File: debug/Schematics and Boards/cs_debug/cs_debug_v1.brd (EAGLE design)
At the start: 83.2 x 62.2 mm, 239 parts, among them J1 J-JTAG-CORTEX_SMD, J19 Solar, J2 J-JTAG-CORTEX_SMD, J3 J-JTAG-CORTEX-NEEDLE6-LEGS, J4 J-SERIAL-PORT, J5 J-WURTH-USBC, Q10 2N7002P, Q3 FDN340P, Q4 2N7002P, Q5 FDN340P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

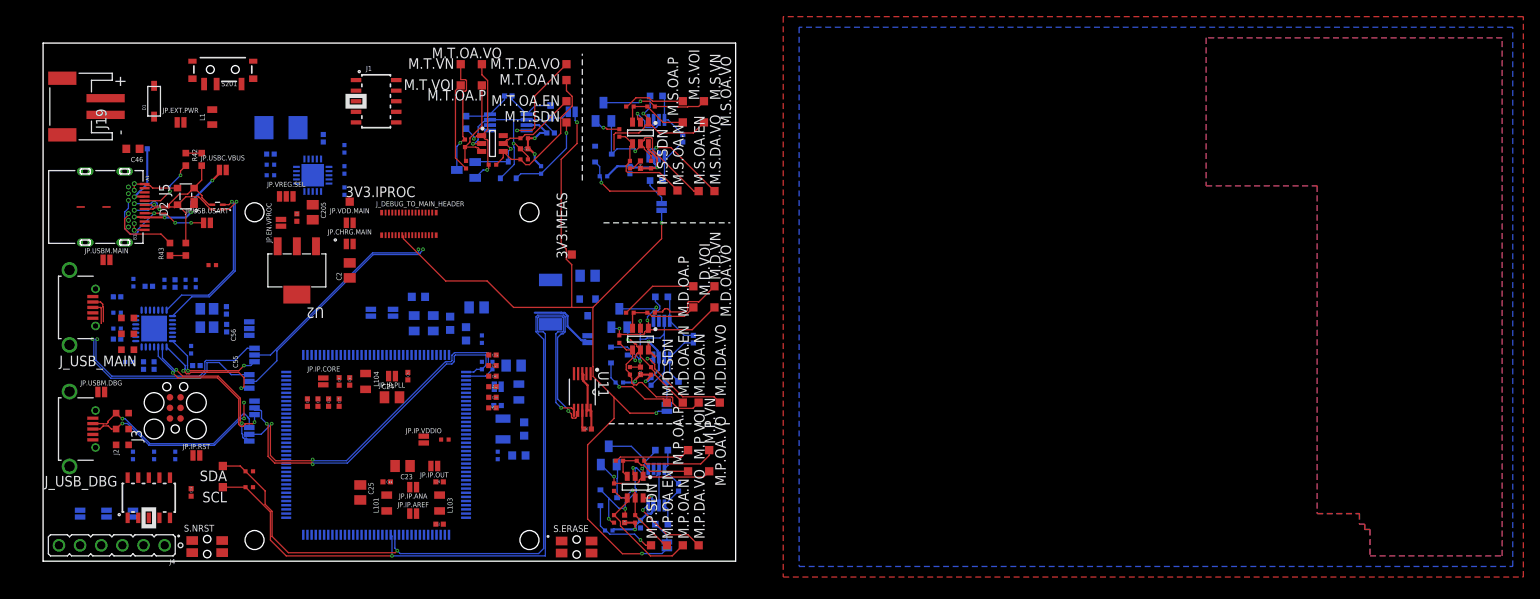
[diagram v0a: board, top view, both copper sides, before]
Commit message: DBG- analog signals hand-routed to go under 0-ohm gnd bridge
Some digital signals that went between planes were not routed under the bridge. There are the signals that  shutdown the opamp that is doing offset biasing. The signals are at about 2 levels removed from any truly analog signals, so any side-effects from ground will be  small beyond perception
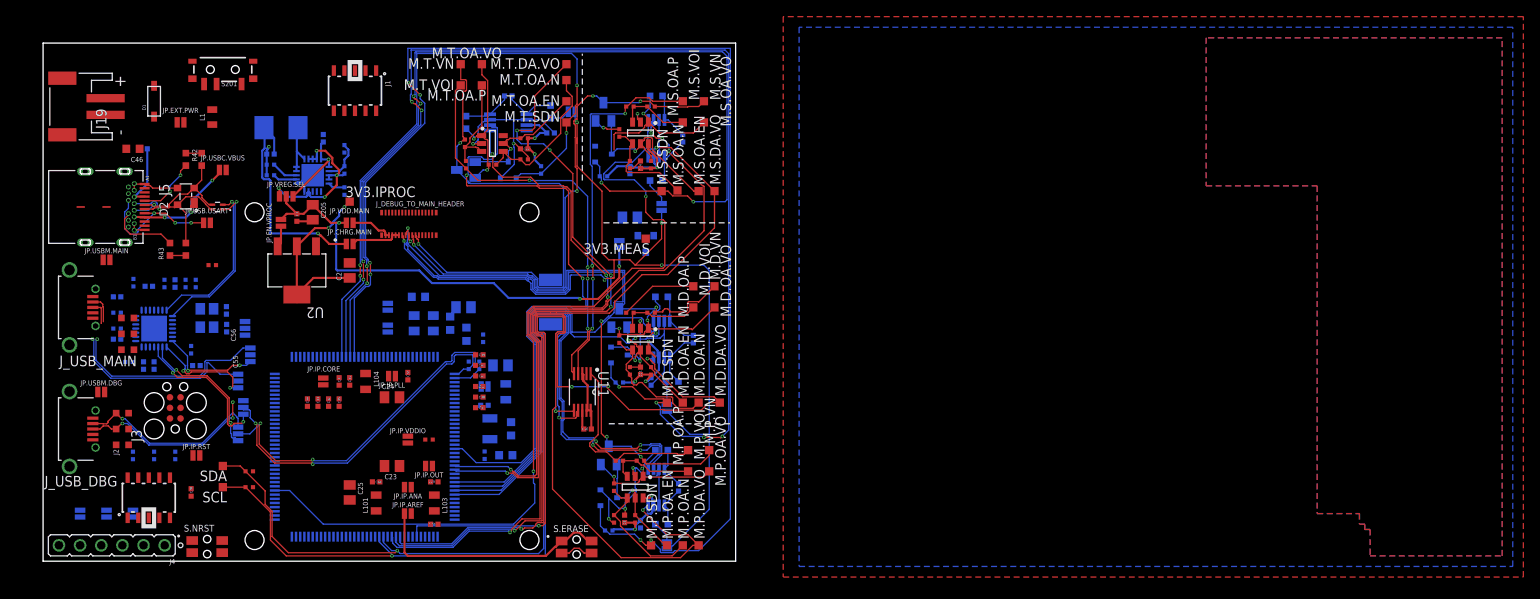
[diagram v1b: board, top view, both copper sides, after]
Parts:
- moved JP.EN.VMEAS 12.0 mm to (46.4, 38.1)
- moved U1 10.3 mm to (49.5, 38.1)
- moved 3V3.MEAS 9.09 mm to (49.5, 38.7), turned to 180 degrees
- moved C1 8.64 mm to (47.6, 41.3)
- moved J1 2.84 mm to (14.6, 56.5), turned to 180 degrees
- moved JP.UART.RX.IP 2.15 mm to (18.5, 30.6)
- moved JP.UART.TX.IP 2.01 mm to (18.5, 27.9)
- moved JP.IP.VDDIO 1.91 mm to (21.0, 14.6)
- moved R41 1.90 mm to (23.5, 14.6)
- moved C26 1.58 mm to (32.1, 23.5)
- moved C27 1.58 mm to (27.6, 30.5)
- moved C37 1.58 mm to (29.5, 18.4)
- moved C38 1.58 mm to (29.5, 19.7)
- moved C39 1.58 mm to (29.5, 24.8)
- moved C40 1.58 mm to (29.5, 23.5)
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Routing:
- net CM_PROC_DCBIAS_SHUTDOWN: track 9.48 -> 159.4 mm, vias 1 -> 6
- net CM_DTR_DCBIAS_SHUTDOWN: track 9.82 -> 147.5 mm, vias 1 -> 8
- net CM_STORAGE_DCBIAS_SHUTDOWN: track 10.4 -> 114.9 mm, vias 1 -> 6
- net CM_STORAGE_DIFFAMP_GAIN0: track 0.00 -> 102.9 mm, vias 0 -> 2
- net CM_PROC_DIFFAMP_OUT: track 9.38 -> 98.2 mm, vias 1 -> 2
- net CM_TEMP_DIFFAMP_OUT: track 12.6 -> 95.4 mm, vias 1 -> 5
- net CM_DTR_DIFFAMP_OUT: track 12.0 -> 91.0 mm, vias 1 -> 4
- net CM_STORAGE_DIFFAMP_OUT: track 10.9 -> 87.1 mm, vias 1 -> 2
- net CM_TEMP_DIFFAMP_GAIN1: track 0.00 -> 74.5 mm, vias 0 -> 2
- net CM_STORAGE_DIFFAMP_GAIN1: track 0.00 -> 72.2 mm, vias 0 -> 4
- net CM_TEMP_DIFFAMP_GAIN0: track 0.00 -> 70.7 mm, vias 0 -> 4
- net CM_TEMP_DCBIAS_SHUTDOWN: track 10.6 -> 78.5 mm, vias 1 -> 4
- net CM_PROC_DIFFAMP_GAIN0: track 0.00 -> 65.6 mm, vias 0 -> 2
- net CM_PROC_DIFFAMP_GAIN1: track 0.00 -> 64.8 mm, vias 0 -> 2
- net CM_PROC_V_SENSE_N: track 14.0 -> 72.1 mm, vias 0 -> 4
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
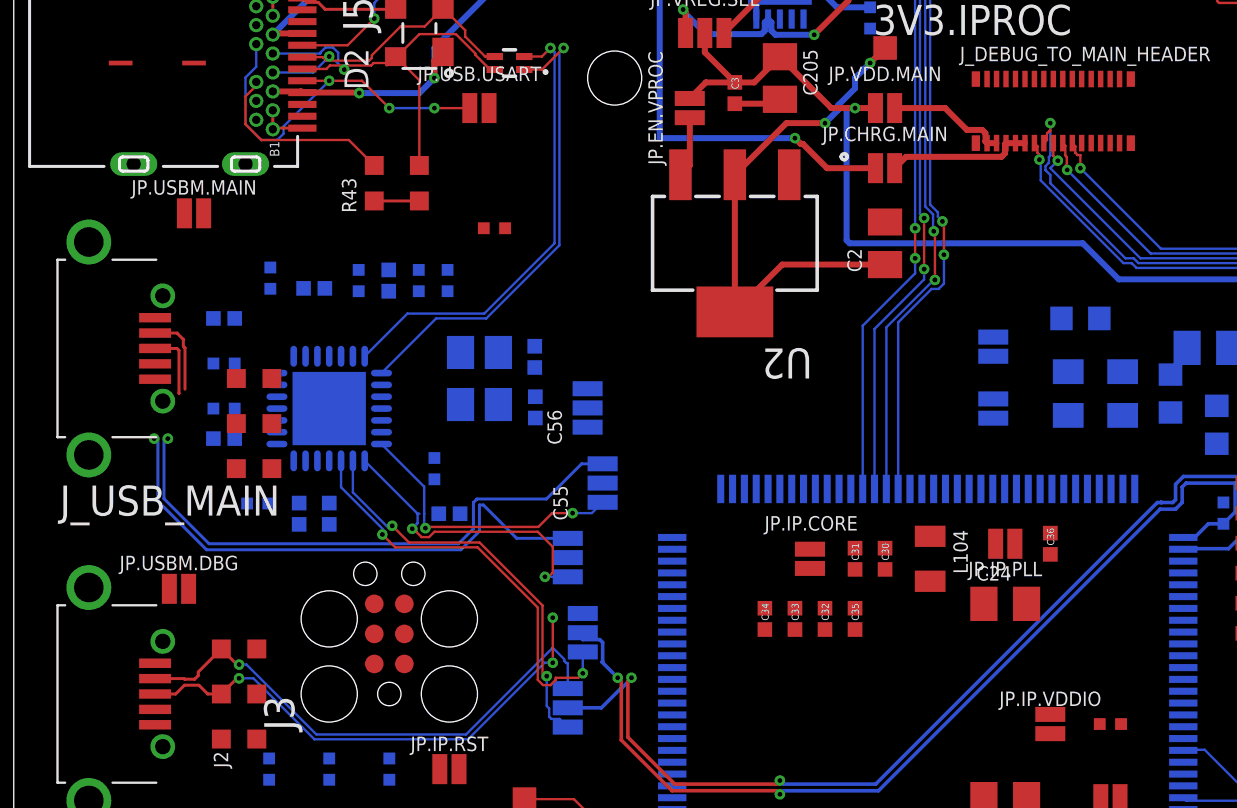
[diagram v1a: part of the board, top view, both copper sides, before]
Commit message: DBG- USB signals finished routing
Differential pairs do wonky things as they try to get identical lengths. I probably violated some rules in this regard, but it should be pretty minimal. Worst offense is the use of 3-pad solder jumpers
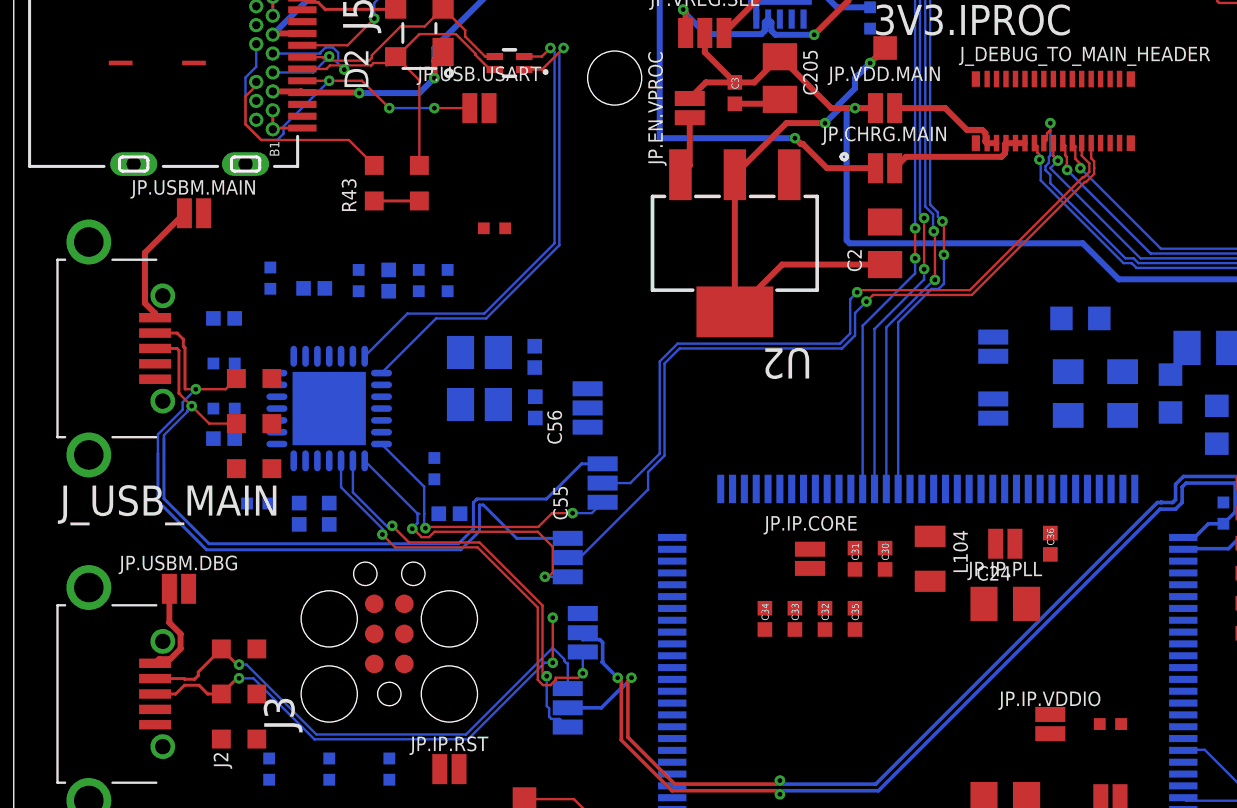
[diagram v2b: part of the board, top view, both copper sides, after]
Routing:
- net MAIN_USB_DATA_P: track 0.51 -> 33.6 mm, vias 0 -> 1
- net MAIN_USB_DATA_N: track 0.00 -> 30.5 mm, vias 0 -> 1
- net USB_BKUP_MAIN_VBUS: track 0.00 -> 5.28 mm
- net USB_BKUP_MAIN_D_N: track 26.4 -> 31.4 mm
- net USB_BKUP_MAIN_D_P: track 26.9 -> 31.6 mm
- net USB_BKUP_DBG_VBUS: track 0.00 -> 4.06 mm

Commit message: DBG - autoroute 100%
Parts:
- moved C27 0.71 mm to (27.7, 31.2)
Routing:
- net 3V3_INSTR_PROC: track 51.7 -> 239.9 mm, vias 2 -> 9
- net MAIN_USART_TX: track 0.00 -> 89.0 mm, vias 0 -> 6
- net AGND: track 85.7 -> 159.9 mm, vias 8 -> 9
- net 3V3_INSTR_MEAS: track 50.1 -> 123.0 mm, vias 8 -> 14
- net MAIN_USART_RX: track 0.00 -> 72.2 mm, vias 0 -> 5
- net VDDOUT_1: track 0.00 -> 69.1 mm, vias 0 -> 5
- net MAIN_GPIO1: track 0.00 -> 63.9 mm, vias 0 -> 5
- net MAIN_GPIO2: track 0.00 -> 61.7 mm, vias 0 -> 5
- net USB_BKUP_DBG_VBUS: track 4.06 -> 65.4 mm, vias 0 -> 1
- net MAIN_TRACE_D0/GPIO6: track 0.00 -> 61.0 mm, vias 0 -> 5
- net MAIN_TRACE_SWO/GPIO5: track 0.00 -> 60.8 mm, vias 0 -> 3
- net MAIN_TRACE_D1/GPIO7: track 0.00 -> 60.6 mm, vias 0 -> 5
- net MAIN_GPIO3: track 0.00 -> 60.4 mm, vias 0 -> 5
- net INSTR_PROC_JTAG_TMS/SWDIO: track 0.00 -> 59.1 mm, vias 0 -> 3
- net INSTR_PROC_NRESET_SW: track 0.00 -> 58.9 mm, vias 0 -> 3
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
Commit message: DBG- DRC errors resolved; due for one more review
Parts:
- moved R48 0.38 mm to (-5.08, 25.8)
- moved C103 0.23 mm to (32.7, 13.0)
- moved VR8 0.18 mm to (-12.9, 29.2)
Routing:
- net DGND: track 71.9 -> 76.1 mm, vias 3 -> 179
- net CM_OPAMP_N2: track 12.7 -> 14.5 mm
- net MAIN_NRESET: track 32.3 -> 34.0 mm
- net VDDOUT_1: track 69.1 -> 70.7 mm
- net AGND: track 159.9 -> 160.7 mm, vias 9 -> 127
- net VDDIO1: track 53.3 -> 53.9 mm
- added copper zone on layer 16, net AGND
- removed copper zone on layer 16, net AGND1

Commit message: DBG-Manual checks & minor cleanup
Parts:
- added JP.HUB.VDD: JUMPER-SMT_2_NC_PASTE_NO-SILK, Connectors:SMT-JUMPER_2_NC_PASTE_NO-SILK
- added R7: 1M, Resistors:R0402
- moved C50 2.15 mm to (-11.6, 22.9), flipped to the top, turned to 180 degrees
- moved S201 1.14 mm to (-1.88, 60.0)
- moved C54 0.86 mm to (-11.6, 23.9), flipped to the top, turned to 180 degrees
- moved JP.USBM.MAIN 0.63 mm to (-15.2, 35.6)
- moved VR7 0.40 mm to (-12.9, 27.7)
- moved VR6 0.25 mm to (-12.9, 25.2)
- renumbered J_DEBUG_TO_MAIN_HEADER to J_DBG_TO_MAIN_HDR
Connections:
- net N$17 renamed USB_RBIAS
- net N$18 renamed HUB_USB_VBUS
- net N$19 renamed USB_HUB_RST
- net N$22 renamed USB_HS_IND
- net N$23 renamed USB_NONRMV1
- net N$24 renamed USB_NONRMV0
- removed net N$20: C55.1, U13.24, Y1.1
- removed net N$21: C56.1, U13.23, Y1.3
- new net USB_HUB_VDD: JP.HUB.VDD.2, U13.10, U13.14, U13.20, U13.27, U13.4
- new net USB_XIN: C55.1, R7.2, U13.24, Y1.1
- new net USB_XOUT: C56.1, R7.1, U13.23, Y1.3
- net 3V3_INSTR_PROC: now also JP.HUB.VDD.1; no longer U13.10, U13.14, U13.20, U13.27, U13.4
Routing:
- net USB_HUB_VDD: track 0.00 -> 24.9 mm, vias 0 -> 5
- net USB_XOUT: track 0.00 -> 8.99 mm
- net N$21: track 7.88 -> 0.00 mm
- net USB_XIN: track 0.00 -> 7.48 mm
- net N$20: track 7.14 -> 0.00 mm
- net 3V3_INSTR_PROC: track 239.9 -> 244.6 mm, vias 9 -> 7
- net DGND: track 76.1 -> 73.7 mm, vias 179 -> 180
- net VSRC_RAW: track 32.8 -> 33.8 mm
- net N$6: track 3.29 -> 4.07 mm
- net USB_BKUP_MAIN_VBUS: track 5.28 -> 4.65 mm
- net VSRC: track 48.6 -> 48.7 mm, vias 0 -> 2

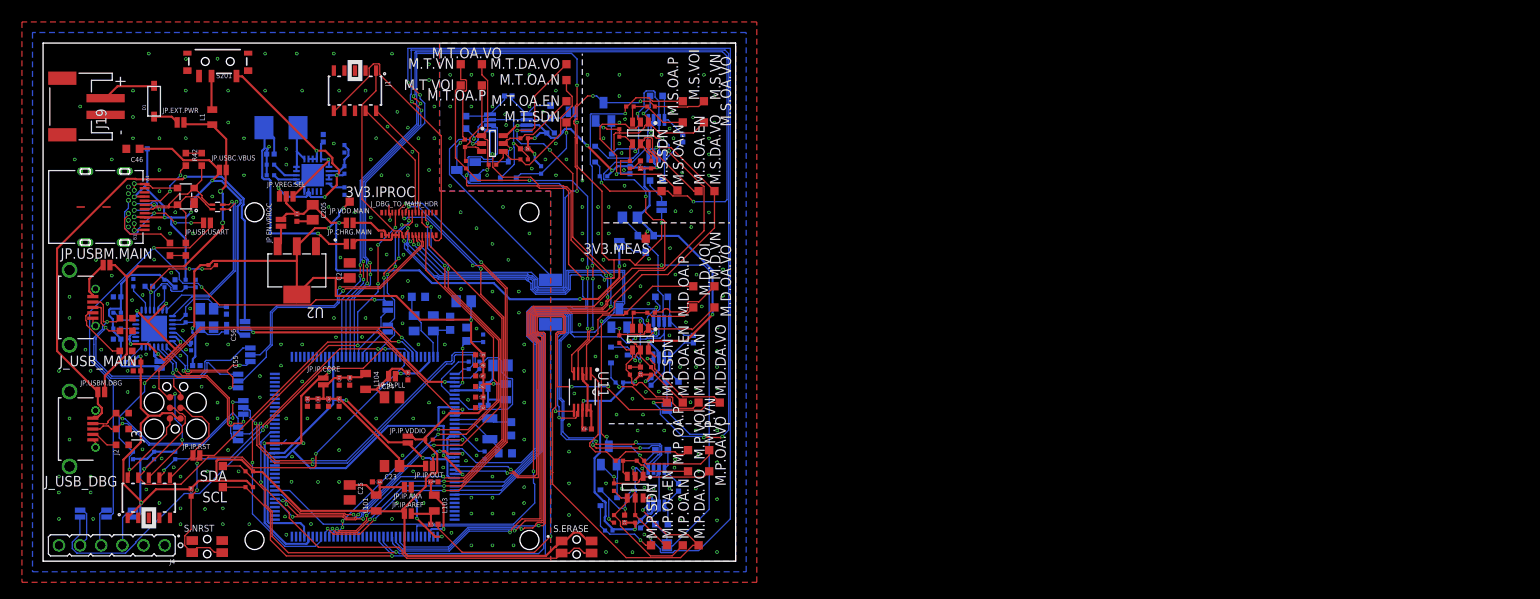
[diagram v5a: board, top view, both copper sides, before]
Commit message: BOM cleanup and initial CAM
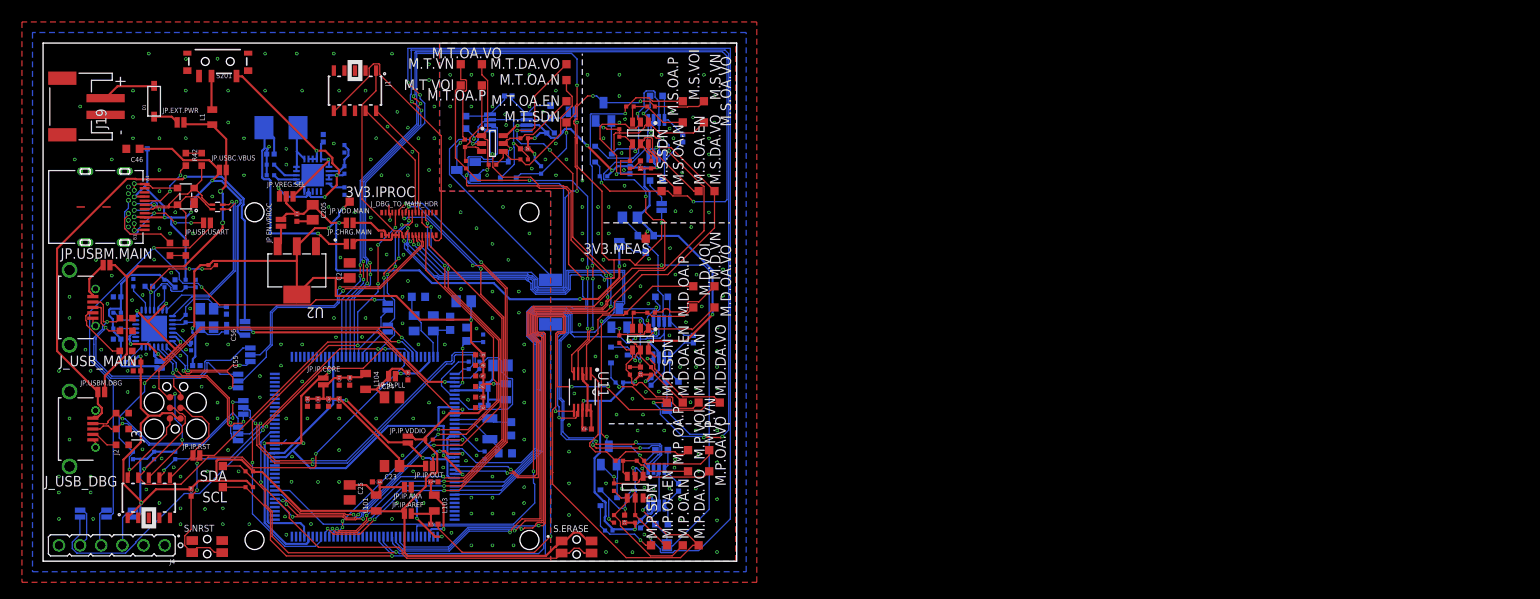
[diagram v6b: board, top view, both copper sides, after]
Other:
- board size 83.2 x 62.2 mm -> 83.3 x 62.2 mm

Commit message: DBG-Cleanup Silkscreen
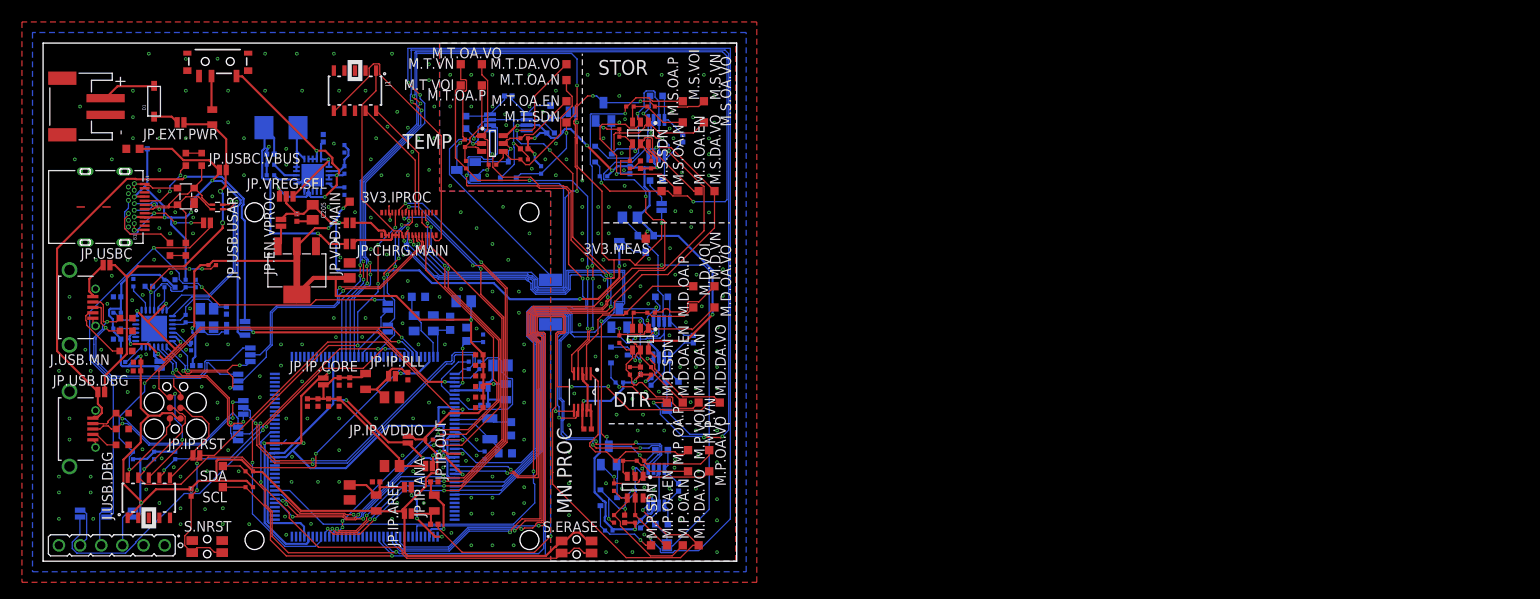
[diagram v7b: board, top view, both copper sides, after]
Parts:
- renumbered JP.USBM.DBG to JP.USB.DBG, JP.USBM.MAIN to JP.USBC, J_USB_DBG to J.USB.DBG, J_USB_MAIN to J.USB.MN
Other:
- board text added: "CommonSense Debug v1 Reese Grimsley CMU-CCSG"
- board text added: "DTR"
- board text added: "MN.PROC"
- board text added: "STOR"
- board text added: "TEMP"

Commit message: DBG-rounded edges
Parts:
- moved J4 0.63 mm to (-14.0, 1.91)
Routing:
- net INSTR_PROC_I2C_SCL: track 94.1 -> 93.3 mm
- net CM_PROC_DIFFAMP_OUT: track 97.9 -> 97.1 mm
- net CM_DTR_DIFFAMP_OUT: track 91.4 -> 90.7 mm
- net INSTR_PROC_I2C_SDA: track 97.0 -> 96.4 mm
- net CM_PROC_DCBIAS_SHUTDOWN: track 160.1 -> 159.5 mm
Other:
- outline, holes or cut-outs redrawn
- board text removed: "CommonSense Debug v1 Reese Grimsley CMU-CCSG"
